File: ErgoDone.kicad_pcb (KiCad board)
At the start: 2 copper layers, 176.6 x 158.9 mm, 150 parts, among them J1 USB, J2 3.5mm, J3 JMP, J4 JMP, SW0:10 SW0:3, SW0:11 SW0:2, SW0:12 SW0:1, SW0:7 SW0:6, SW0:8 SW0:5, SW0:9 SW0:4, SW1:10 SW1:3, SW1:11 SW1:2, SW1:12 SW1:1, SW1:13 SW1:0, SW1:9 SW1:4, SW2:10 SW2:3, SW2:11 SW2:2, SW2:12 SW2:1, SW2:13 SW2:0, SW2:7 SW2:6, SW2:8 SW2:5, SW2:9 SW2:4, SW3:10 SW3:3, SW3:11 SW3:2, SW3:12 SW3:1, SW3:13 SW3:0, SW3:7 SW3:6, SW3:8 SW3:5, SW3:9 SW3:4, SW4:10 SW4:3, SW4:11 SW4:2, SW4:12 SW4:1, SW4:13 SW4:0, SW4:7 SW4:6, SW4:8 SW4:5, SW4:9 SW4:4, SW5:10 SW5:3, SW5:11 SW5:2, SW5:12 SW5:1, SW5:13 SW5:0, SW5:7 SW5:6, SW5:8 SW5:5, SW5:9 SW5:4, U1 ProMicro, U2 MCP23017

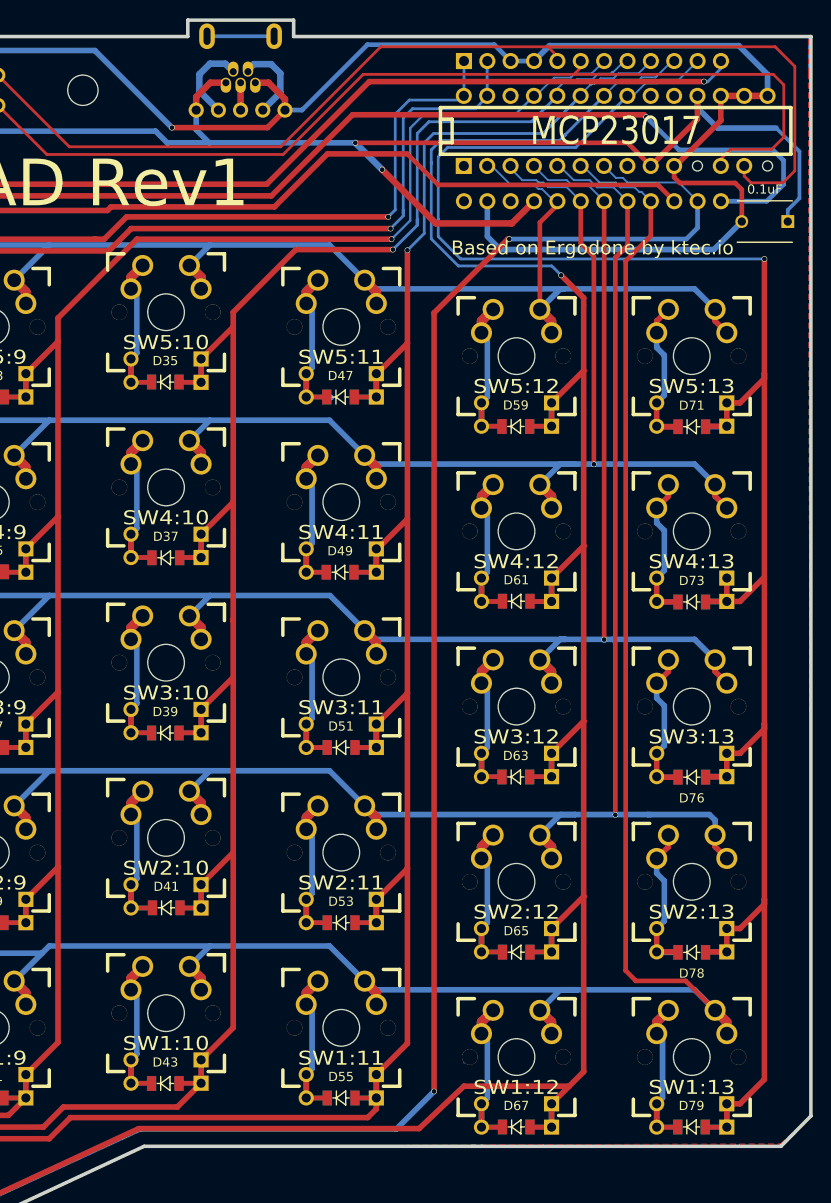
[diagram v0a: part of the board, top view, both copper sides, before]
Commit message: Moving chips and narrowing PCB
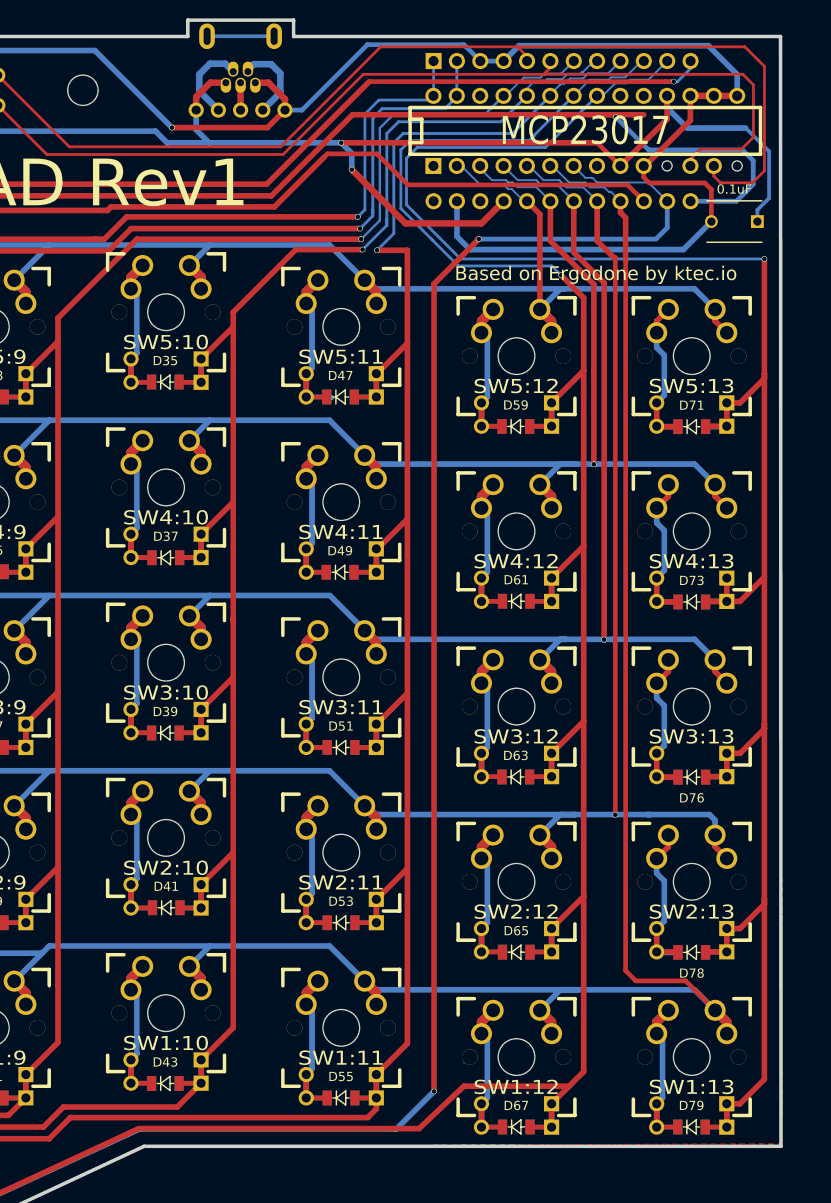
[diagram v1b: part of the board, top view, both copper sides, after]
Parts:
- removed G***: LOGO, ErgoDox_pro_micro_edition:ergo_icon
- moved U1 3.30 mm to (172.6, 42.5)
- moved C1 3.30 mm to (193.8, 52.4)
- moved U2 3.30 mm to (175.1, 42.5)
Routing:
- net VCC: track 177.8 -> 173.7 mm
- net /COL6: track 310.4 -> 307.1 mm
- net GND: track 226.5 -> 223.2 mm
- net /SDAM: track 154.4 -> 151.1 mm
- net /COL5: track 256.2 -> 252.9 mm
- net /COL4: track 314.3 -> 311.0 mm
- net /COL11: track 302.0 -> 305.3 mm
- net /COL10: track 273.7 -> 270.4 mm
- net /LED_C: track 119.7 -> 116.4 mm
- net /LED_A: track 128.4 -> 125.1 mm
- net /SCLM: track 137.0 -> 133.9 mm
- net /ROW3: track 231.6 -> 233.5 mm
- net /COL1: track 352.0 -> 353.4 mm
- net /ROW4: track 216.5 -> 217.9 mm
- net /ROW0: track 411.9 -> 410.6 mm
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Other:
- board size 176.6 x 158.9 mm -> 173.3 x 158.9 mm

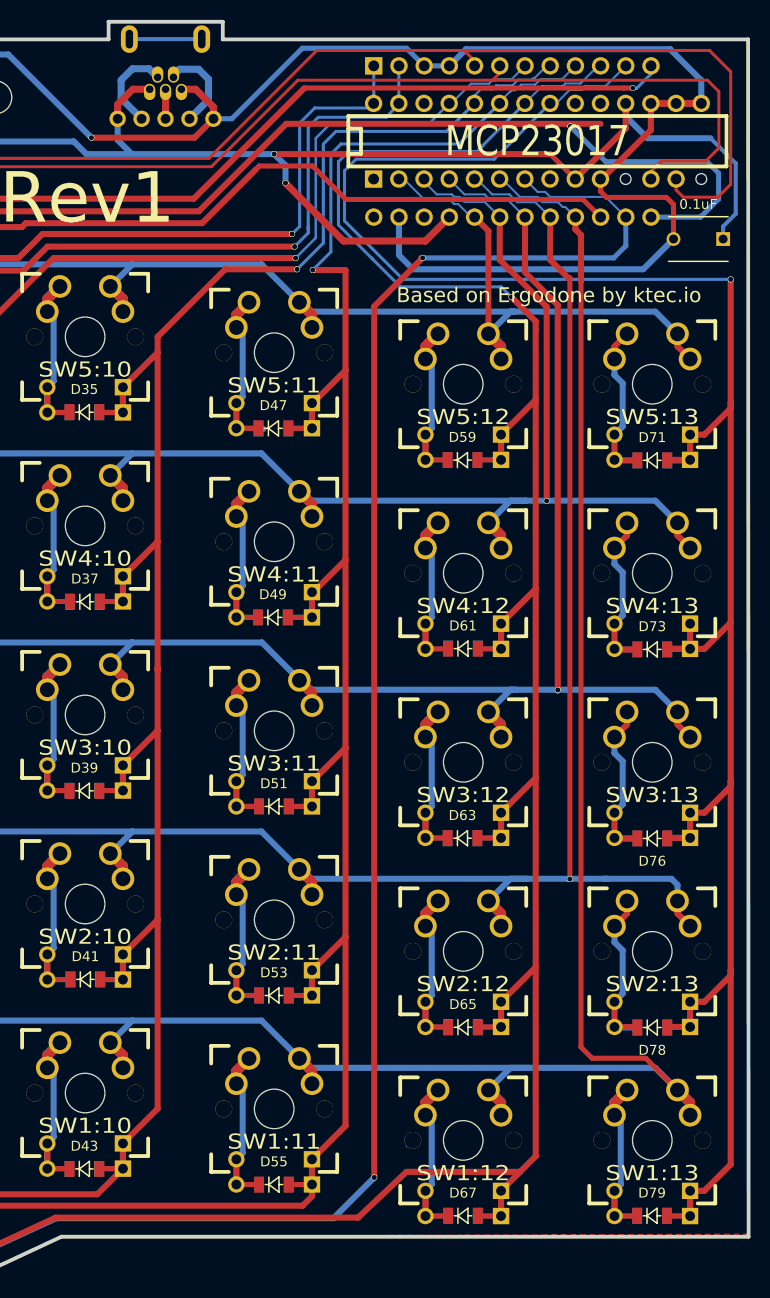
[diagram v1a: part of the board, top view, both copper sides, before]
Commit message: Chamfering corners and generating up-to date gerber files including updated drill maps.
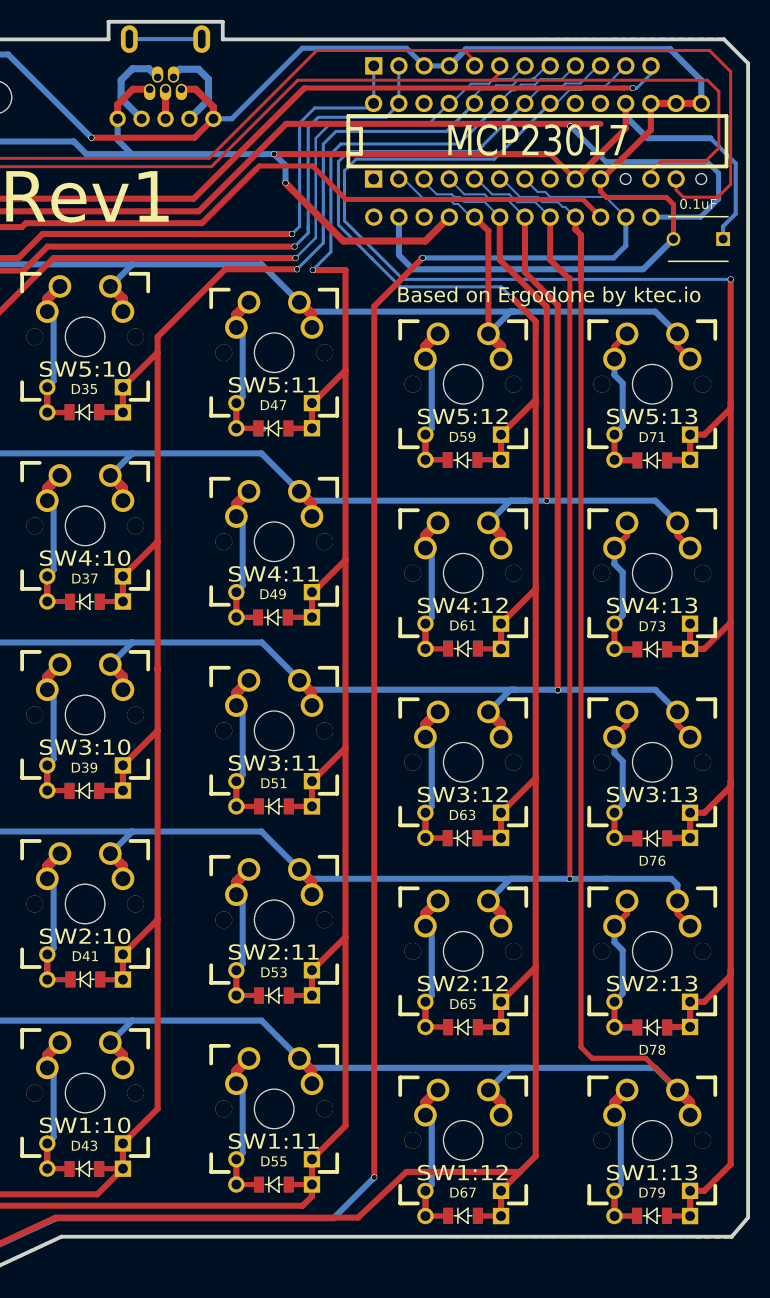
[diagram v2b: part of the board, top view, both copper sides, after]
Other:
- outline, holes or cut-outs redrawn
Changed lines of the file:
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@@
   (general
     (thickness 1.6002)
-    (drawings 42)
+    (drawings 44)
     (tracks 1644)
     (zones 0)
@@
   (page A4)
   (layers
-    (0 Front signal hide)
-    (31 Back signal hide)
+    (0 Front signal)
+    (31 Back signal)
     (32 B.Adhes user hide)
     (33 F.Adhes user hide)
@@
     (39 F.Mask user)
     (40 Dwgs.User user)
-    (41 Cmts.User user hide)
-    (42 Eco1.User user hide)
-    (43 Eco2.User user hide)
+    (41 Cmts.User user)
+    (42 Eco1.User user)
+    (43 Eco2.User user)
     (44 Edge.Cuts user)
   )
   (setup
-    (last_trace_width 0.508)
+    (last_trace_width 0.3048)
     (user_trace_width 0.03302)
     (user_trace_width 0.1524)
@@
     (visible_elements 7FFFFFFF)
     (pcbplotparams
-      (layerselection 0x010f0_ffffffff)
+      (layerselection 0x010fc_ffffffff)
       (usegerberextensions false)
       (usegerberattributes false)
@@
       (net 7 /COL6))
   )
+  (gr_line (start 196.215 151.13) (end 194.691 152.908) (layer Edge.Cuts) (width 0.381))
+  (gr_line (start 196.342 34.671) (end 193.929 32.258) (layer Edge.Cuts) (width 0.381))
   (gr_text + (at 69.2404 37.3888) (layer B.SilkS)
     (effects (font (size 1.524 1.524) (thickness 0.15)) (justify mirror))
@@
     (effects (font (size 2.032 1.524) (thickness 0.3048)) (justify left))
   )
-  (gr_line (start 127.1524 152.908) (end 196.3928 152.908) (angle 90) (layer Edge.Cuts) (width 0.381))
-  (gr_line (start 196.3928 152.908) (end 196.342 32.258) (angle 90) (layer Edge.Cuts) (width 0.381))
-  (gr_line (start 196.342 32.258) (end 143.4084 32.258) (angle 90) (layer Edge.Cuts) (width 0.381))
+  (gr_line (start 127.1524 152.908) (end 194.691 152.908) (angle 90) (layer Edge.Cuts) (width 0.381))
+  (gr_line (start 196.342 151.003) (end 196.342 34.671) (angle 90) (layer Edge.Cuts) (width 0.381))
+  (gr_line (start 193.929 32.258) (end 143.4084 32.258) (angle 90) (layer Edge.Cuts) (width 0.381))
   (gr_line (start 143.4084 32.258) (end 143.4084 30.48) (angle 90) (layer Edge.Cuts) (width 0.381))
   (gr_line (start 143.4084 30.48) (end 131.9022 30.48) (angle 90) (layer Edge.Cuts) (width 0.381))
@@
     (polygon
       (pts
-        (xy 48.9839 189.35192) (xy 127.1524 152.908) (xy 196.342 152.654) (xy 196.469 149.225) (xy 196.342 36.322)
-        (xy 196.342 32.258) (xy 143.4084 32.258) (xy 143.4084 30.48) (xy 131.9022 30.48) (xy 131.9022 32.258)
+        (xy 48.9839 189.35192) (xy 127.1524 152.908) (xy 194.691 152.908) (xy 196.342 151.13) (xy 196.342 34.671)
+        (xy 193.802 32.131) (xy 143.4084 32.258) (xy 143.4084 30.48) (xy 131.9022 30.48) (xy 131.9022 32.258)
         (xy 95.0468 32.258) (xy 95.0468 30.48) (xy 88.7095 30.48) (xy 88.7095 31.75) (xy 84.2137 31.75)
         (xy 84.2137 30.48) (xy 77.8764 30.48) (xy 77.8764 32.258) (xy 65.8114 32.258) (xy 62.611 35.433)
@@
     (polygon
       (pts
-        (xy 48.9839 189.35192) (xy 127.1524 152.908) (xy 196.3928 152.908) (xy 196.469 148.463) (xy 196.342 35.814)
-        (xy 196.342 32.258) (xy 143.4084 32.258) (xy 143.4084 30.48) (xy 131.9022 30.48) (xy 131.9022 32.258)
+        (xy 48.9839 189.35192) (xy 127.1524 152.908) (xy 194.691 153.035) (xy 196.342 151.003) (xy 196.342 34.671)
+        (xy 193.802 32.131) (xy 143.4084 32.258) (xy 143.4084 30.48) (xy 131.9022 30.48) (xy 131.9022 32.258)
         (xy 95.0468 32.258) (xy 95.0468 30.48) (xy 88.7095 30.48) (xy 88.7095 31.75) (xy 84.2137 31.75)
         (xy 84.2137 30.48) (xy 77.8764 30.48) (xy 77.8764 32.258) (xy 65.8114 32.258) (xy 62.611 35.433)

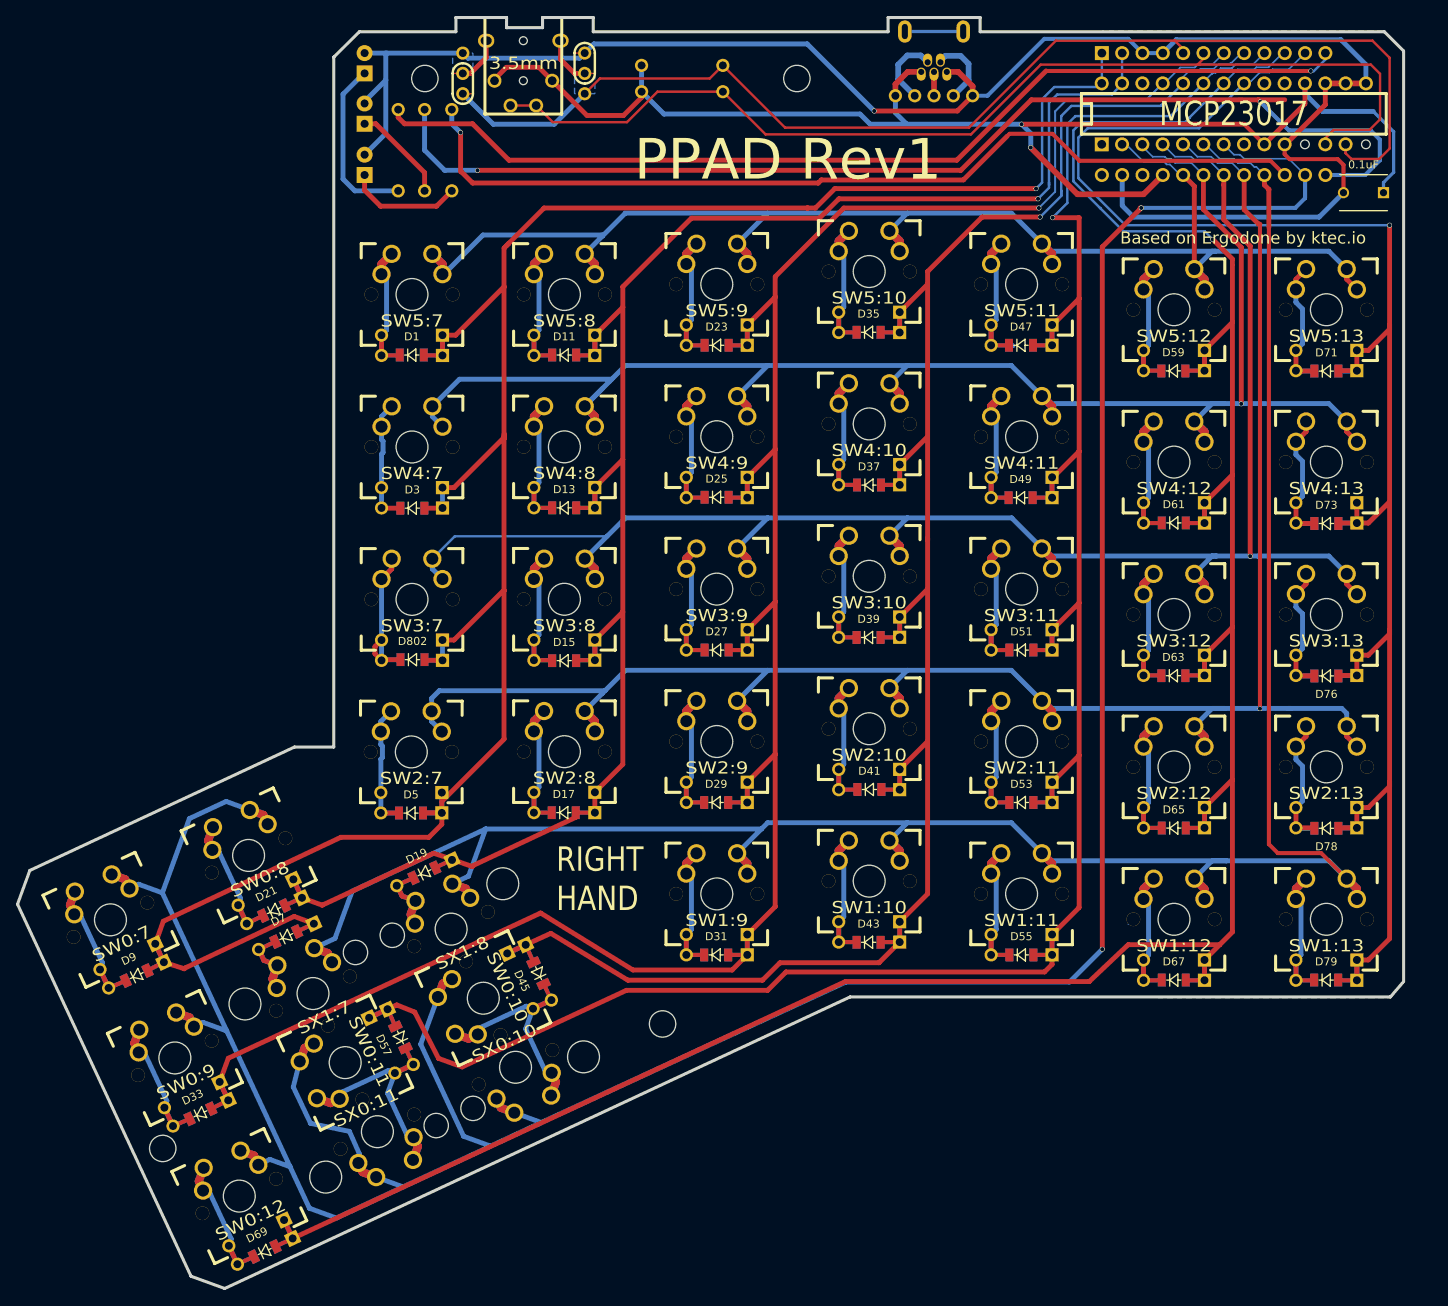
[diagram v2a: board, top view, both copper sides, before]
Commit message: Correcting edge cuts to close the gap in pcb cut.
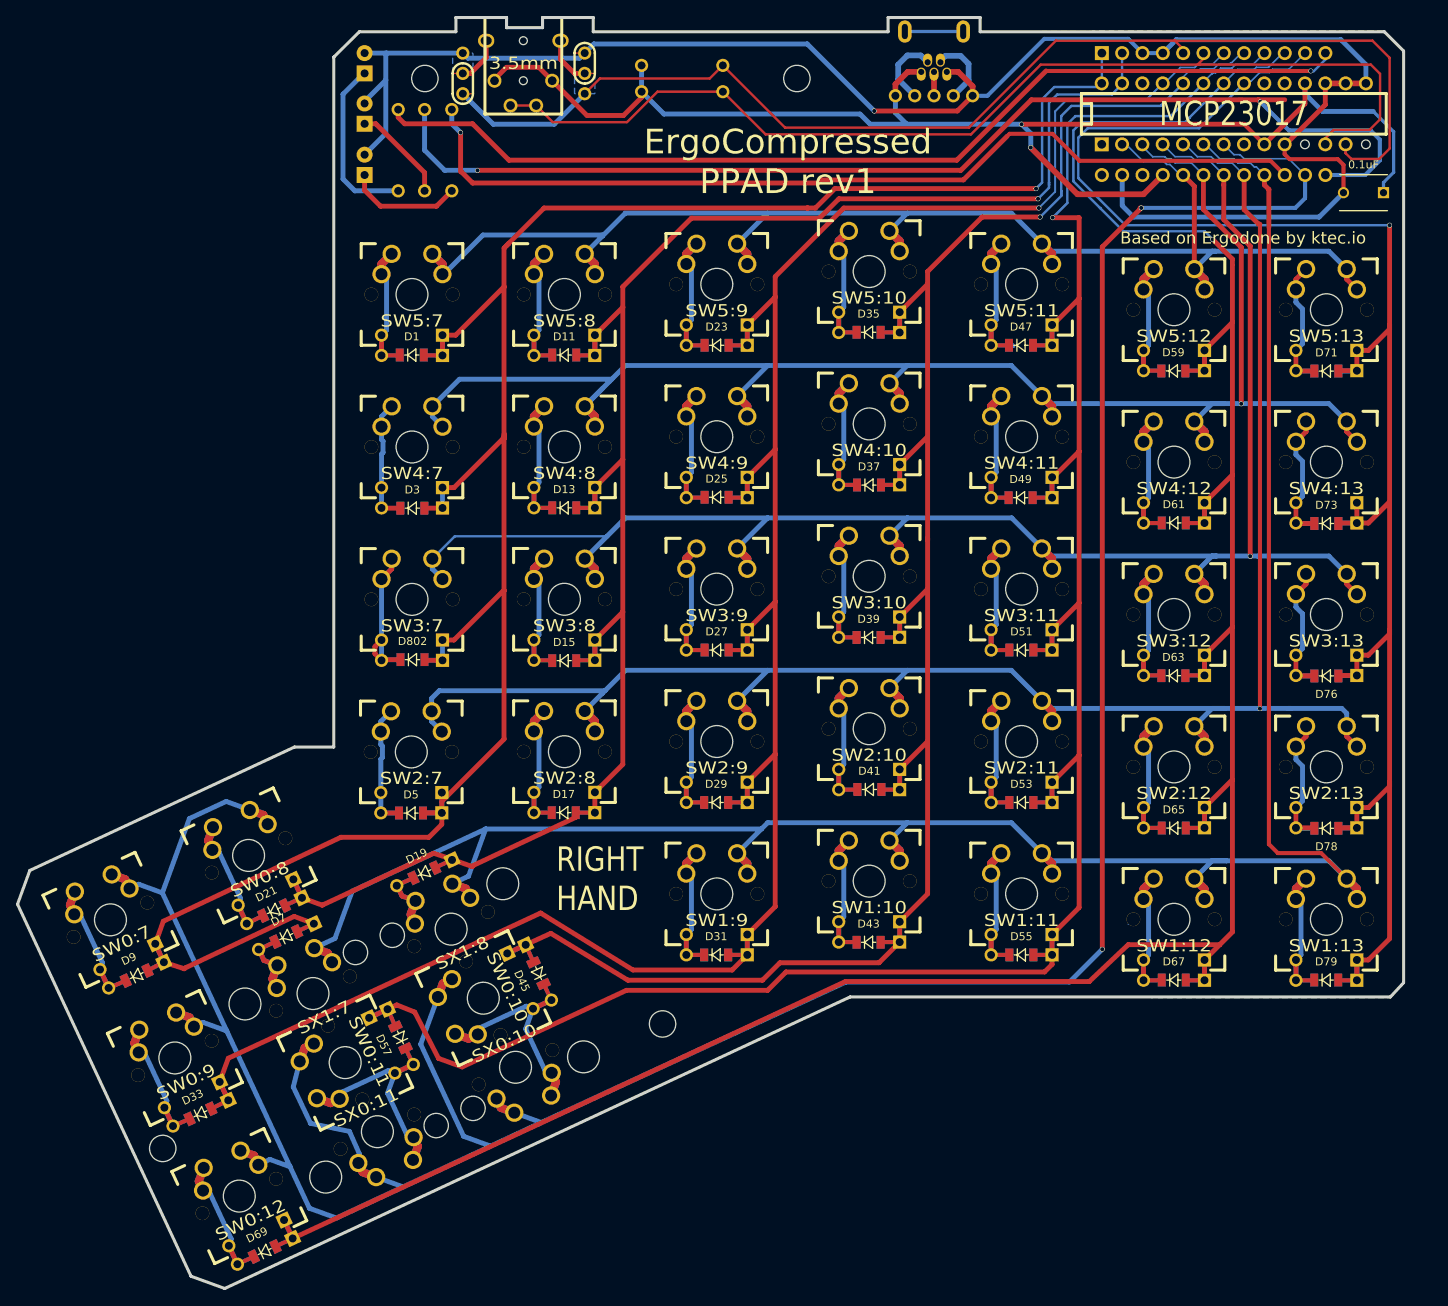
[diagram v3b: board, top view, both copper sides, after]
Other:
- outline, holes or cut-outs redrawn
- board text added: "ErgoCompressed PPAD rev1"
- board text removed: "PPAD Rev1"
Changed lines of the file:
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@@
-(kicad_pcb (version 20171130) (host pcbnew "(5.0.1)-rc2")
+(kicad_pcb (version 20171130) (host pcbnew "(5.0.1)-3")
   (general
     (thickness 1.6002)
@@
     (0 Front signal)
     (31 Back signal)
-    (32 B.Adhes user hide)
-    (33 F.Adhes user hide)
-    (34 B.Paste user hide)
-    (35 F.Paste user hide)
+    (32 B.Adhes user)
+    (33 F.Adhes user)
+    (34 B.Paste user)
+    (35 F.Paste user)
     (36 B.SilkS user)
     (37 F.SilkS user)
@@
       (net 7 /COL6))
   )
-  (gr_line (start 196.215 151.13) (end 194.691 152.908) (layer Edge.Cuts) (width 0.381))
+  (gr_line (start 196.342 151.13) (end 194.691 152.908) (layer Edge.Cuts) (width 0.381))
   (gr_line (start 196.342 34.671) (end 193.929 32.258) (layer Edge.Cuts) (width 0.381))
   (gr_text + (at 69.2404 37.3888) (layer B.SilkS)
@@
     (effects (font (size 2.032 1.524) (thickness 0.3048)) (justify mirror))
   )
-  (gr_text "PPAD Rev1" (at 119.38 48.26) (layer F.SilkS)
-    (effects (font (size 5.08 5.08) (thickness 1.27)))
+  (gr_text "ErgoCompressed \nPPAD rev1" (at 119.38 48.514) (layer F.SilkS)
+    (effects (font (size 3.08 3.08) (thickness 0.57)))
   )
   (gr_text "Ver 1.4" (at 83.82 53.34) (layer B.SilkS)
@@
   )
   (gr_line (start 127.1524 152.908) (end 194.691 152.908) (angle 90) (layer Edge.Cuts) (width 0.381))
-  (gr_line (start 196.342 151.003) (end 196.342 34.671) (angle 90) (layer Edge.Cuts) (width 0.381))
+  (gr_line (start 196.342 151.13) (end 196.342 34.671) (angle 90) (layer Edge.Cuts) (width 0.381))
   (gr_line (start 193.929 32.258) (end 143.4084 32.258) (angle 90) (layer Edge.Cuts) (width 0.381))
   (gr_line (start 143.4084 32.258) (end 143.4084 30.48) (angle 90) (layer Edge.Cuts) (width 0.381))
